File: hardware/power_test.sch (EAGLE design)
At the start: 45 parts, among them J10 USB-MICROA-AMPHENOL-10118192-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, J3 USB-MICROB-EDAC-690-005-299-0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, U1 DPDT-X2, U3 FT232RLSSOP, U4 MCP73831T-2ACI/OT

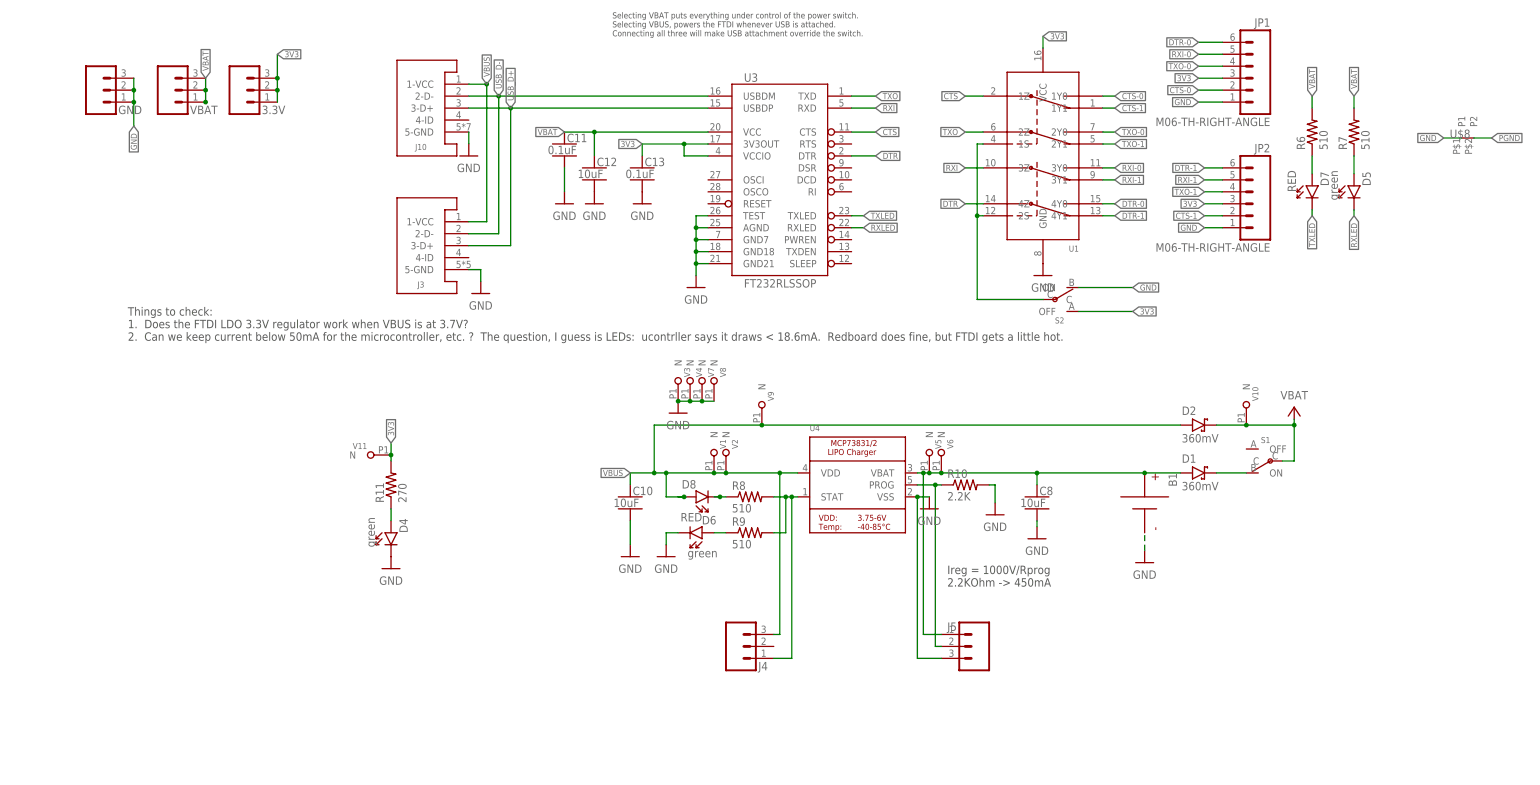
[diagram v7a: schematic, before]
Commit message: verified 3.7V opertaion of ftdi regulator.  checked circuit on bread board
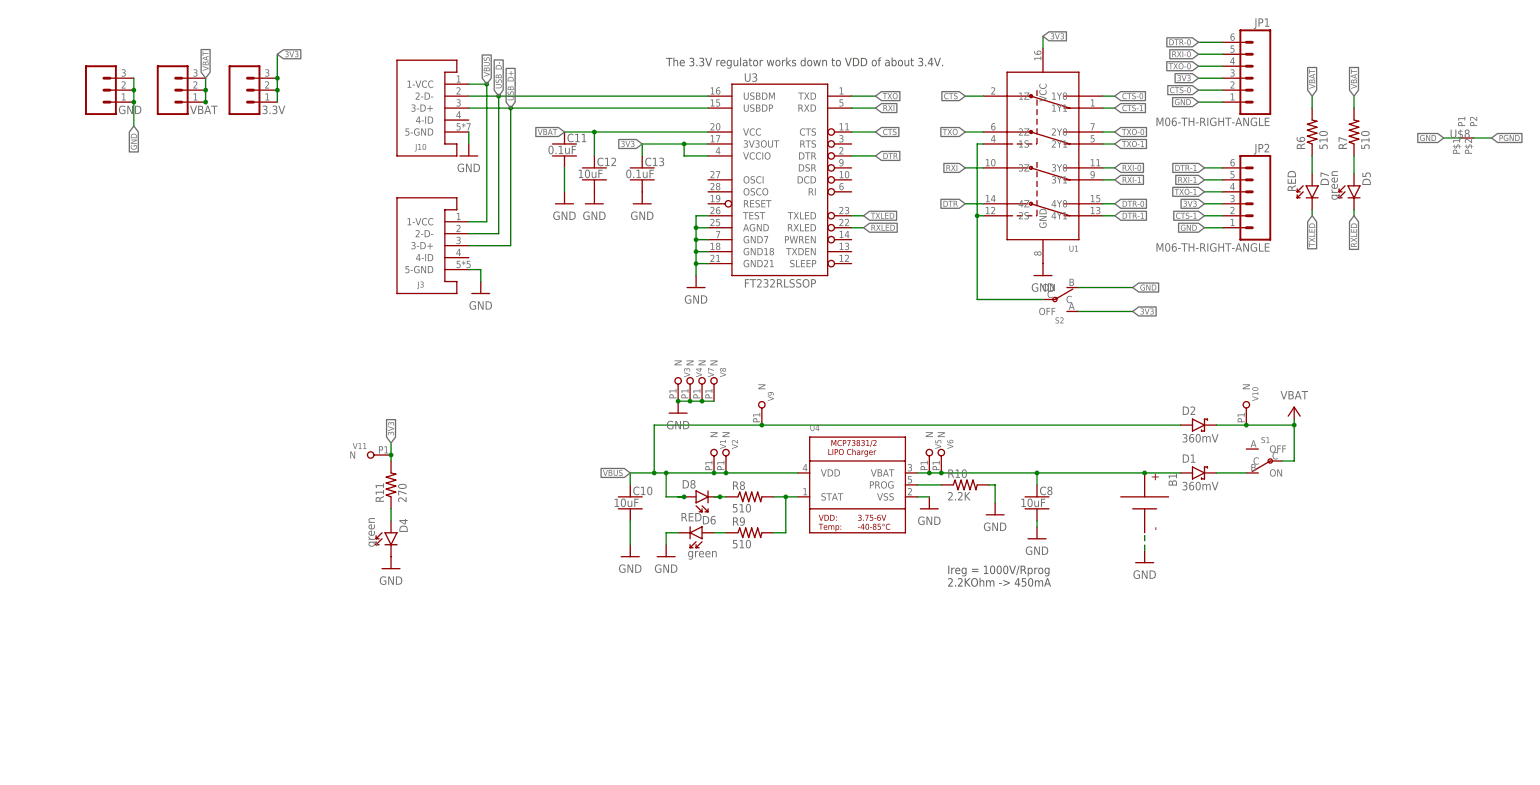
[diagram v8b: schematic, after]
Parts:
- removed J4, J5: (no value), Components:HEADER-0.1IN-3POS-MALE
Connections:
- net BPOS: no longer J5.1
- net GND: no longer J5.3
- net N$11: no longer J4.1
- net N$12: no longer J5.2
- net VBUS: no longer J4.3
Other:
- note added: "The 3.3V regulator works down to VDD of about 3.4V."
- note removed: "Selecting VBAT puts everything under control of the power switch. Selecting VBUS, powers the FTDI whenever USB is attached. Connecting all three will make USB attachment override the switch."
- note removed: "Things to check: 1. Does the FTDI LDO 3.3V regulator work when VBUS is at 3.7V? 2. Can we keep current below 50mA for the microcontroller, etc. ? The question, I guess is LEDs: ucontrller says it draws < 18.6mA. Redboard does fine, but FTDI gets a little hot."
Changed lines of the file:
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@@
 <setting verticaltext="up"/>
 </settings>
-<grid distance="0.05" unitdist="inch" unit="inch" style="lines" multiple="1" display="no" altdistance="0.01" altunitdist="inch" altunit="inch"/>
+<grid distance="0.1" unitdist="inch" unit="inch" style="lines" multiple="1" display="no" altdistance="0.01" altunitdist="inch" altunit="inch"/>
 <layers>
 <layer number="99" name="SpiceOrder" color="7" fill="1" visible="no" active="no"/>
@@
 <part name="D2" library="quadparts_prebuilt" deviceset="DIODE-SCHOTTKY_" device="SMD-SOD123-360MV" value="360mV"/>
 <part name="GND4" library="quadparts_prebuilt" deviceset="GND" device=""/>
-<part name="J4" library="Components" deviceset="HEADER-0.1IN-3POS" device="-MALE">
-<attribute name="PIN1" value="STAT"/>
-<attribute name="PIN2" value=""/>
-<attribute name="PIN3" value="VDD"/>
-</part>
-<part name="J5" library="Components" deviceset="HEADER-0.1IN-3POS" device="-MALE">
-<attribute name="PIN1" value="VBAT"/>
-<attribute name="PIN2" value="PROG"/>
-<attribute name="PIN3" value="VSS"/>
-</part>
 <part name="V9" library="quadparts_prebuilt" deviceset="LOCKED-VIA" device="-0.2"/>
 <part name="V10" library="quadparts_prebuilt" deviceset="LOCKED-VIA" device="-0.2"/>
@@
 <text x="204.47" y="153.67" size="1.778" layer="97">Ireg = 1000V/Rprog
 2.2KOhm -&gt; 450mA</text>
-<text x="133.35" y="270.51" size="1.27" layer="97">Selecting VBAT puts everything under control of the power switch.
-Selecting VBUS, powers the FTDI whenever USB is attached.
-Connecting all three will make USB attachment override the switch.</text>
-<text x="30.48" y="203.2" size="1.778" layer="97">Things to check:
-1.  Does the FTDI LDO 3.3V regulator work when VBUS is at 3.7V?
-2.  Can we keep current below 50mA for the microcontroller, etc. ?  The question, I guess is LEDs:  ucontrller says it draws &lt; 18.6mA.  Redboard does fine, but FTDI gets a little hot.
-</text>
+<text x="144.78" y="264.16" size="1.778" layer="97">The 3.3V regulator works down to VDD of about 3.4V.</text>
 </plain>
 <instances>
@@
 <instance part="D2" gate="G$1" x="259.08" y="187.96"/>
 <instance part="GND4" gate="1" x="105.41" y="215.9"/>
-<instance part="J4" gate="G$1" x="157.48" y="135.89"/>
-<instance part="J5" gate="G$1" x="213.36" y="146.05" rot="R180"/>
 <instance part="V9" gate="G$1" x="165.1" y="187.96" rot="R90"/>
 <instance part="V10" gate="G$1" x="267.97" y="187.96" rot="R90"/>
@@
 <pinref part="U4" gate="G$1" pin="VSS"/>
 <wire x1="198.12" y1="172.72" x2="200.66" y2="172.72" width="0.1524" layer="91"/>
-<pinref part="J5" gate="G$1" pin="3"/>
-<wire x1="198.12" y1="172.72" x2="198.12" y2="138.43" width="0.1524" layer="91"/>
-<wire x1="198.12" y1="138.43" x2="203.2" y2="138.43" width="0.1524" layer="91"/>
-<junction x="198.12" y="172.72"/>
 </segment>
 <segment>
@@
 <wire x1="223.52" y1="177.8" x2="203.2" y2="177.8" width="0.1524" layer="91"/>
 <wire x1="203.2" y1="177.8" x2="200.66" y2="177.8" width="0.1524" layer="91"/>
-<wire x1="200.66" y1="177.8" x2="199.39" y2="177.8" width="0.1524" layer="91"/>
-<wire x1="199.39" y1="177.8" x2="198.12" y2="177.8" width="0.1524" layer="91"/>
+<wire x1="200.66" y1="177.8" x2="198.12" y2="177.8" width="0.1524" layer="91"/>
 <wire x1="223.52" y1="175.26" x2="223.52" y2="177.8" width="0.1524" layer="91"/>
 <junction x="223.52" y="177.8"/>
@@
 <wire x1="223.52" y1="177.8" x2="246.38" y2="177.8" width="0.1524" layer="91"/>
 <junction x="246.38" y="177.8"/>
-<pinref part="J5" gate="G$1" pin="1"/>
-<wire x1="199.39" y1="177.8" x2="199.39" y2="143.51" width="0.1524" layer="91"/>
-<wire x1="199.39" y1="143.51" x2="203.2" y2="143.51" width="0.1524" layer="91"/>
-<junction x="199.39" y="177.8"/>
 </segment>
 </net>
@@
 <wire x1="167.64" y1="172.72" x2="170.18" y2="172.72" width="0.1524" layer="91"/>
 <pinref part="R9" gate="G$1" pin="2"/>
-<wire x1="170.18" y1="172.72" x2="171.45" y2="172.72" width="0.1524" layer="91"/>
-<wire x1="171.45" y1="172.72" x2="172.72" y2="172.72" width="0.1524" layer="91"/>
+<wire x1="170.18" y1="172.72" x2="172.72" y2="172.72" width="0.1524" layer="91"/>
 <wire x1="167.64" y1="165.1" x2="170.18" y2="165.1" width="0.1524" layer="91"/>
 <wire x1="170.18" y1="165.1" x2="170.18" y2="172.72" width="0.1524" layer="91"/>
 <junction x="170.18" y="172.72"/>
-<pinref part="J4" gate="G$1" pin="1"/>
-<wire x1="171.45" y1="172.72" x2="171.45" y2="138.43" width="0.1524" layer="91"/>
-<wire x1="171.45" y1="138.43" x2="167.64" y2="138.43" width="0.1524" layer="91"/>
-<junction x="171.45" y="172.72"/>
 </segment>
 </net>
@@
 <segment>
 <pinref part="U4" gate="G$1" pin="PROG"/>
-<wire x1="198.12" y1="175.26" x2="201.93" y2="175.26" width="0.1524" layer="91"/>
+<wire x1="198.12" y1="175.26" x2="203.2" y2="175.26" width="0.1524" layer="91"/>
 <pinref part="R10" gate="G$1" pin="1"/>
-<pinref part="J5" gate="G$1" pin="2"/>
-<wire x1="201.93" y1="175.26" x2="203.2" y2="175.26" width="0.1524" layer="91"/>
-<wire x1="201.93" y1="175.26" x2="201.93" y2="140.97" width="0.1524" layer="91"/>
-<wire x1="201.93" y1="140.97" x2="203.2" y2="140.97" width="0.1524" layer="91"/>
-<junction x="201.93" y="175.26"/>
 </segment>
 </net>
@@
 <wire x1="144.78" y1="177.8" x2="154.94" y2="177.8" width="0.1524" layer="91"/>
 <wire x1="154.94" y1="177.8" x2="157.48" y2="177.8" width="0.1524" layer="91"/>
-<wire x1="157.48" y1="177.8" x2="168.91" y2="177.8" width="0.1524" layer="91"/>
-<wire x1="168.91" y1="177.8" x2="172.72" y2="177.8" width="0.1524" layer="91"/>
+<wire x1="157.48" y1="177.8" x2="172.72" y2="177.8" width="0.1524" layer="91"/>
 <wire x1="137.16" y1="175.26" x2="137.16" y2="177.8" width="0.1524" layer="91"/>
 <wire x1="147.32" y1="172.72" x2="148.59" y2="172.72" width="0.1524" layer="91"/>
@@
 <junction x="142.24" y="177.8"/>
 <pinref part="D2" gate="G$1" pin="A"/>
-<pinref part="J4" gate="G$1" pin="3"/>
 <wire x1="165.1" y1="187.96" x2="254" y2="187.96" width="0.1524" layer="91"/>
-<wire x1="168.91" y1="177.8" x2="168.91" y2="143.51" width="0.1524" layer="91"/>
-<wire x1="168.91" y1="143.51" x2="167.64" y2="143.51" width="0.1524" layer="91"/>
-<junction x="168.91" y="177.8"/>
 <pinref part="V9" gate="G$1" pin="N"/>
 <junction x="165.1" y="187.96"/>
